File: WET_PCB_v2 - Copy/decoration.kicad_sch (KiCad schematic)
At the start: 24 parts, among them J19 Fuse holder or smth to hold t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, J20 Fuse holder or smth to hold t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, J21 Fuse holder or smth to hold t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, J22 Fuse holder or smth to hold t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, J23 Fuse holder or smth to hold t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, J24 Fuse holder or smth to hold t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, J25 Fuse holder or smth to hold t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, J26 Fuse holder or smth to hold t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, J27 Fuse holder or smth to hold t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, J28 Fuse holder or smth to hold t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, J29 Fuse holder or smth to hold t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, J30 Fuse holder or smth to hold t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

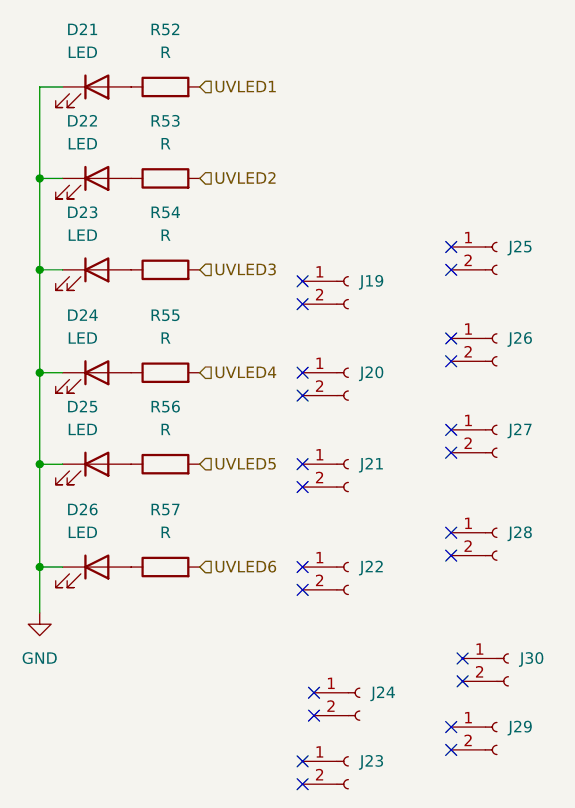
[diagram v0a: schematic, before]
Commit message: microcontroller to chip traces done
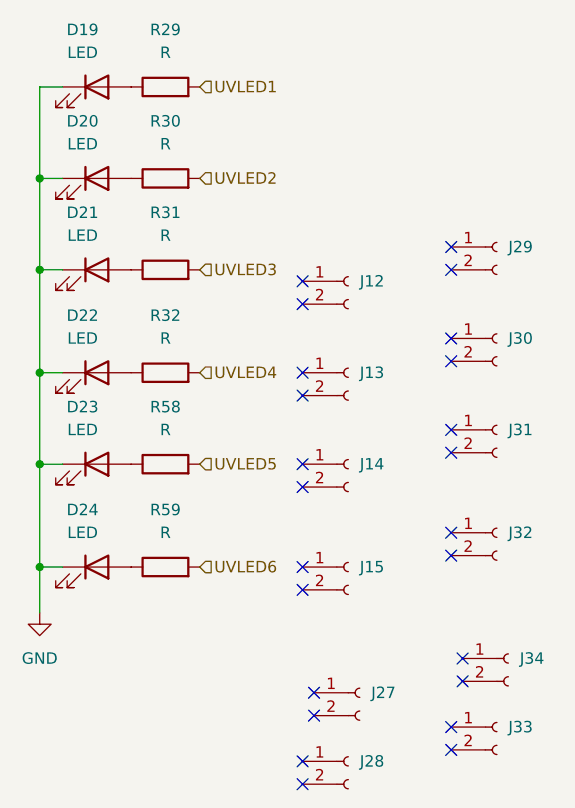
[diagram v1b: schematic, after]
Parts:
- renumbered D21 to D19, D22 to D20, D23 to D21, D24 to D22, D25 to D23, D26 to D24, J19 to J12, J20 to J13, J21 to J14, J22 to J15, J24 to J27, J23 to J28, J25 to J29, J26 to J30, J27 to J31, J28 to J32, J29 to J33, J30 to J34, R52 to R29, R53 to R30, R54 to R31, R55 to R32, R56 to R58, R57 to R59
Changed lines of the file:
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@@
 		(dnp no)
 		(fields_autoplaced yes)
-		(property "Reference" "R57"
+		(property "Reference" "R59"
 			(at 119.38 101.6 90)
 			(show_name no)
@@
 			(project "WET_PCB_v2"
 				(path "/13451c35-1666-47d9-9525-8d8125ba1cf3/79e5e86e-dc26-4d0b-a087-2027a5880c08"
-					(reference "R57")
+					(reference "R59")
 					(unit 1)
 				)
@@
 		(dnp no)
 		(fields_autoplaced yes)
-		(property "Reference" "R53"
+		(property "Reference" "R30"
 			(at 119.38 58.42 90)
 			(show_name no)
@@
 			(project "WET_PCB_v2"
 				(path "/13451c35-1666-47d9-9525-8d8125ba1cf3/79e5e86e-dc26-4d0b-a087-2027a5880c08"
-					(reference "R53")
+					(reference "R30")
 					(unit 1)
 				)
@@
 		(dnp no)
 		(fields_autoplaced yes)
-		(property "Reference" "J23"
+		(property "Reference" "J28"
 			(at 140.97 129.5399 0)
 			(show_name no)
@@
 			(project "WET_PCB_v2"
 				(path "/13451c35-1666-47d9-9525-8d8125ba1cf3/79e5e86e-dc26-4d0b-a087-2027a5880c08"
-					(reference "J23")
+					(reference "J28")
 					(unit 1)
 				)
@@
 		(dnp no)
 		(fields_autoplaced yes)
-		(property "Reference" "J19"
+		(property "Reference" "J12"
 			(at 140.97 76.1999 0)
 			(show_name no)
@@
 			(project "WET_PCB_v2"
 				(path "/13451c35-1666-47d9-9525-8d8125ba1cf3/79e5e86e-dc26-4d0b-a087-2027a5880c08"
-					(reference "J19")
+					(reference "J12")
 					(unit 1)
 				)
@@
 		(dnp no)
 		(fields_autoplaced yes)
-		(property "Reference" "D25"
+		(property "Reference" "D23"
 			(at 110.1725 90.17 0)
 			(show_name no)
@@
 			(project "WET_PCB_v2"
 				(path "/13451c35-1666-47d9-9525-8d8125ba1cf3/79e5e86e-dc26-4d0b-a087-2027a5880c08"
-					(reference "D25")
+					(reference "D23")
 					(unit 1)
 				)
@@
 		(dnp no)
 		(fields_autoplaced yes)
-		(property "Reference" "R55"
+		(property "Reference" "R32"
 			(at 119.38 80.01 90)
 			(show_name no)
@@
 			(project "WET_PCB_v2"
 				(path "/13451c35-1666-47d9-9525-8d8125ba1cf3/79e5e86e-dc26-4d0b-a087-2027a5880c08"
-					(reference "R55")
+					(reference "R32")
 					(unit 1)
 				)
@@
 		(dnp no)
 		(fields_autoplaced yes)
-		(property "Reference" "J21"
+		(property "Reference" "J14"
 			(at 140.97 96.5199 0)
 			(show_name no)
@@
 			(project "WET_PCB_v2"
 				(path "/13451c35-1666-47d9-9525-8d8125ba1cf3/79e5e86e-dc26-4d0b-a087-2027a5880c08"
-					(reference "J21")
+					(reference "J14")
 					(unit 1)
 				)
@@
 		(dnp no)
 		(fields_autoplaced yes)
-		(property "Reference" "R52"
+		(property "Reference" "R29"
 			(at 119.38 48.26 90)
 			(show_name no)
@@
 			(project "WET_PCB_v2"
 				(path "/13451c35-1666-47d9-9525-8d8125ba1cf3/79e5e86e-dc26-4d0b-a087-2027a5880c08"
-					(reference "R52")
+					(reference "R29")
 					(unit 1)
 				)
@@
 		(dnp no)
 		(fields_autoplaced yes)
-		(property "Reference" "D24"
+		(property "Reference" "D22"
 			(at 110.1725 80.01 0)
 			(show_name no)
@@
 			(project "WET_PCB_v2"
 				(path "/13451c35-1666-47d9-9525-8d8125ba1cf3/79e5e86e-dc26-4d0b-a087-2027a5880c08"
-					(reference "D24")
+					(reference "D22")
 					(unit 1)
 				)
@@
 		(dnp no)
 		(fields_autoplaced yes)
-		(property "Reference" "#PWR062"
+		(property "Reference" "#PWR05"
 			(at 105.41 119.38 0)
 			(hide yes)
@@
 			(project "WET_PCB_v2"
 				(path "/13451c35-1666-47d9-9525-8d8125ba1cf3/79e5e86e-dc26-4d0b-a087-2027a5880c08"
-					(reference "#PWR062")
+					(reference "#PWR05")
 					(unit 1)
 				)
@@
 		(dnp no)
 		(fields_autoplaced yes)
-		(property "Reference" "J26"
+		(property "Reference" "J30"
 			(at 157.48 82.5499 0)
 			(show_name no)
@@
 			(project "WET_PCB_v2"
 				(path "/13451c35-1666-47d9-9525-8d8125ba1cf3/79e5e86e-dc26-4d0b-a087-2027a5880c08"
-					(reference "J26")
+					(reference "J30")
 					(unit 1)
 				)
@@
 		(dnp no)
 		(fields_autoplaced yes)
-		(property "Reference" "J30"
+		(property "Reference" "J34"
 			(at 158.75 118.1099 0)
 			(show_name no)
@@
 			(project "WET_PCB_v2"
 				(path "/13451c35-1666-47d9-9525-8d8125ba1cf3/79e5e86e-dc26-4d0b-a087-2027a5880c08"
-					(reference "J30")
+					(reference "J34")
 					(unit 1)
 				)
@@
 		(dnp no)
 		(fields_autoplaced yes)
-		(property "Reference" "J25"
+		(property "Reference" "J29"
 			(at 157.48 72.3899 0)
 			(show_name no)
@@
 			(project "WET_PCB_v2"
 				(path "/13451c35-1666-47d9-9525-8d8125ba1cf3/79e5e86e-dc26-4d0b-a087-2027a5880c08"
-					(reference "J25")
+					(reference "J29")
 					(unit 1)
 				)
@@
 		(dnp no)
 		(fields_autoplaced yes)
-		(property "Reference" "D21"
+		(property "Reference" "D19"
 			(at 110.1725 48.26 0)
 			(show_name no)
@@
 			(project "WET_PCB_v2"
 				(path "/13451c35-1666-47d9-9525-8d8125ba1cf3/79e5e86e-dc26-4d0b-a087-2027a5880c08"
-					(reference "D21")
+					(reference "D19")
 					(unit 1)
 				)
@@
 		(dnp no)
 		(fields_autoplaced yes)
-		(property "Reference" "R56"
+		(property "Reference" "R58"
 			(at 119.38 90.17 90)
 			(show_name no)
@@
 			(project "WET_PCB_v2"
 				(path "/13451c35-1666-47d9-9525-8d8125ba1cf3/79e5e86e-dc26-4d0b-a087-2027a5880c08"
-					(reference "R56")
+					(reference "R58")
 					(unit 1)
 				)
@@
 		(dnp no)
 		(fields_autoplaced yes)
-		(property "Reference" "J22"
+		(property "Reference" "J15"
 			(at 140.97 107.9499 0)
 			(show_name no)
@@
 			(project "WET_PCB_v2"
 				(path "/13451c35-1666-47d9-9525-8d8125ba1cf3/79e5e86e-dc26-4d0b-a087-2027a5880c08"
-					(reference "J22")
+					(reference "J15")
 					(unit 1)
 				)
@@
 		(dnp no)
 		(fields_autoplaced yes)
-		(property "Reference" "J20"
+		(property "Reference" "J13"
 			(at 140.97 86.3599 0)
 			(show_name no)
@@
 			(project "WET_PCB_v2"
 				(path "/13451c35-1666-47d9-9525-8d8125ba1cf3/79e5e86e-dc26-4d0b-a087-2027a5880c08"
-					(reference "J20")
+					(reference "J13")
 					(unit 1)
 				)
@@
 		(dnp no)
 		(fields_autoplaced yes)
-		(property "Reference" "D22"
+		(property "Reference" "D20"
 			(at 110.1725 58.42 0)
 			(show_name no)
@@
 			(project "WET_PCB_v2"
 				(path "/13451c35-1666-47d9-9525-8d8125ba1cf3/79e5e86e-dc26-4d0b-a087-2027a5880c08"
-					(reference "D22")
+					(reference "D20")
 					(unit 1)
 				)
@@
 		(dnp no)
 		(fields_autoplaced yes)
-		(property "Reference" "J29"
+		(property "Reference" "J33"
 			(at 157.48 125.7299 0)
 			(show_name no)
@@
 			(project "WET_PCB_v2"
 				(path "/13451c35-1666-47d9-9525-8d8125ba1cf3/79e5e86e-dc26-4d0b-a087-2027a5880c08"
-					(reference "J29")
+					(reference "J33")
 					(unit 1)
 				)
@@
 		(dnp no)
 		(fields_autoplaced yes)
-		(property "Reference" "D26"
+		(property "Reference" "D24"
 			(at 110.1725 101.6 0)
 			(show_name no)
@@
 			(project "WET_PCB_v2"
 				(path "/13451c35-1666-47d9-9525-8d8125ba1cf3/79e5e86e-dc26-4d0b-a087-2027a5880c08"
-					(reference "D26")
+					(reference "D24")
 					(unit 1)
 				)
@@
 		(dnp no)
 		(fields_autoplaced yes)
-		(property "Reference" "D23"
+		(property "Reference" "D21"
 			(at 110.1725 68.58 0)
 			(show_name no)
@@
 			(project "WET_PCB_v2"
 				(path "/13451c35-1666-47d9-9525-8d8125ba1cf3/79e5e86e-dc26-4d0b-a087-2027a5880c08"
-					(reference "D23")
+					(reference "D21")
 					(unit 1)
 				)
@@
 		(dnp no)
 		(fields_autoplaced yes)
-		(property "Reference" "J24"
+		(property "Reference" "J27"
 			(at 142.24 121.9199 0)
 			(show_name no)
@@
 			(project "WET_PCB_v2"
 				(path "/13451c35-1666-47d9-9525-8d8125ba1cf3/79e5e86e-dc26-4d0b-a087-2027a5880c08"
-					(reference "J24")
+					(reference "J27")
 					(unit 1)
 				)
@@
 		(dnp no)
 		(fields_autoplaced yes)
-		(property "Reference" "R54"
+		(property "Reference" "R31"
 			(at 119.38 68.58 90)
 			(show_name no)
@@
 			(project "WET_PCB_v2"
 				(path "/13451c35-1666-47d9-9525-8d8125ba1cf3/79e5e86e-dc26-4d0b-a087-2027a5880c08"
-					(reference "R54")
+					(reference "R31")
 					(unit 1)
 				)
@@
 		(dnp no)
 		(fields_autoplaced yes)
-		(property "Reference" "J28"
+		(property "Reference" "J32"
 			(at 157.48 104.1399 0)
 			(show_name no)
@@
 			(project "WET_PCB_v2"
 				(path "/13451c35-1666-47d9-9525-8d8125ba1cf3/79e5e86e-dc26-4d0b-a087-2027a5880c08"
-					(reference "J28")
+					(reference "J32")
 					(unit 1)
 				)
@@
 		(dnp no)
 		(fields_autoplaced yes)
-		(property "Reference" "J27"
+		(property "Reference" "J31"
 			(at 157.48 92.7099 0)
 			(show_name no)
@@
 			(project "WET_PCB_v2"
 				(path "/13451c35-1666-47d9-9525-8d8125ba1cf3/79e5e86e-dc26-4d0b-a087-2027a5880c08"
-					(reference "J27")
-					(unit 1)
-				)
+					(reference "J31")
+					(unit 1)
+				)
